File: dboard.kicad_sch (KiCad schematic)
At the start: 10 parts, among them J1 USB_C_Receptacle_USB2.0, J2 Conn_01x04_MountingPin

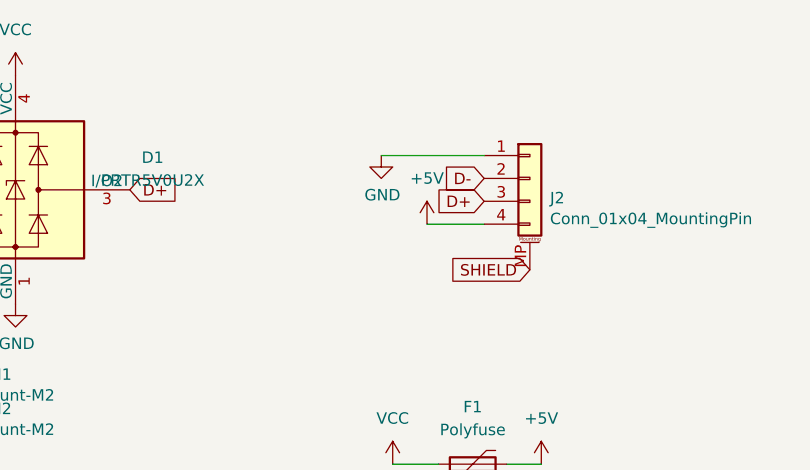
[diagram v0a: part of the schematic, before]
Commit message: fixed pinout
made pinout udb compatible
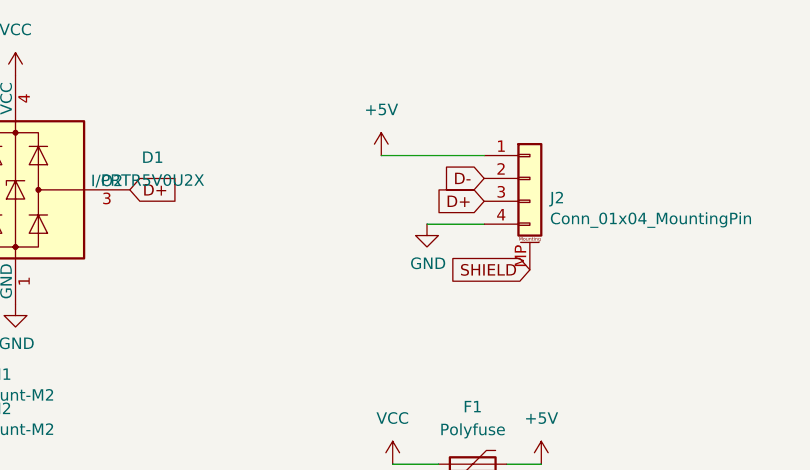
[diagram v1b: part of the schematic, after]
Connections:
- net +5V: now also J2.1 (Pin_1); no longer J2.4 (Pin_4)
- net GND: now also J2.4 (Pin_4); no longer J2.1 (Pin_1)
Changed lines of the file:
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@@
     (pin "1")
   )
-  (symbol (lib_id "power:GND") (at 127 30.48 0) (unit 1)
+  (symbol (lib_id "power:GND") (at 132.08 38.1 0) (unit 1)
     (in_bom yes) (on_board yes)
-    (property "Reference" "#PWR01" (id 0) (at 127 36.83 0)
+    (property "Reference" "#PWR01" (id 0) (at 132.08 44.45 0)
       (effects (font (size 1.27 1.27)) hide)
     )
-    (property "Value" "GND" (id 1) (at 127.127 34.8742 0))
-    (property "Footprint" "" (id 2) (at 127 30.48 0)
+    (property "Value" "GND" (id 1) (at 132.207 42.4942 0))
+    (property "Footprint" "" (id 2) (at 132.08 38.1 0)
       (effects (font (size 1.27 1.27)) hide)
     )
-    (property "Datasheet" "" (id 3) (at 127 30.48 0)
+    (property "Datasheet" "" (id 3) (at 132.08 38.1 0)
       (effects (font (size 1.27 1.27)) hide)
     )
@@
     (pin "1")
   )
-  (symbol (lib_id "power:+5V") (at 132.08 38.1 0) (unit 1)
-    (in_bom yes) (on_board yes) (fields_autoplaced)
-    (property "Reference" "#PWR0104" (id 0) (at 132.08 41.91 0)
+  (symbol (lib_id "power:+5V") (at 127 30.48 0) (unit 1)
+    (in_bom yes) (on_board yes)
+    (property "Reference" "#PWR0104" (id 0) (at 127 34.29 0)
       (effects (font (size 1.27 1.27)) hide)
     )
-    (property "Value" "+5V" (id 1) (at 132.08 33.02 0))
-    (property "Footprint" "" (id 2) (at 132.08 38.1 0)
+    (property "Value" "+5V" (id 1) (at 127 25.4 0))
+    (property "Footprint" "" (id 2) (at 127 30.48 0)
       (effects (font (size 1.27 1.27)) hide)
     )
-    (property "Datasheet" "" (id 3) (at 132.08 38.1 0)
+    (property "Datasheet" "" (id 3) (at 127 30.48 0)
       (effects (font (size 1.27 1.27)) hide)
     )
